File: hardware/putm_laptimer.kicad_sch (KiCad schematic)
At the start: 46 parts, among them J1 Conn_01x22, J10 Conn_01x07, J11 Conn_01x07, J12 Conn_01x09, J13 Conn_01x01, J14 Conn_01x01, J15 Conn_01x01, J16 Conn_01x01, J2 Conn_01x22, J3 Conn_01x22, J4 Conn_01x22, J5 2601-3109, J6 2601-3109, J7 Conn_02x05_Odd_Even, J8 2601-1103, J9 2601-1102

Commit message: Fixed bom table
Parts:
- C1, C10, C3, C4, C5, C6, C7, C8, C9: Mouser Part Number 81-GRM33R6YA104ME14D -> (none); Mouser/TME part number (none) -> 81-GRM33R6YA104ME14D
- D1: Mouser Part Number 621-DESD3V3L2BTQ-7 -> (none); Mouser/TME part number (none) -> 621-DESD3V3L2BTQ-7
- D2: Mouser Part Number 621-MBR230S1F-7 -> (none); Mouser/TME part number (none) -> 621-MBR230S1F-7
- J1, J2, J3, J4: Mouser Part Number ZL262-40SG -> (none); Mouser/TME part number (none) -> ZL262-40SG
- J10, J11: Mouser Part Number ZL262-7SG -> (none); Mouser/TME part number (none) -> ZL262-7SG
- J12: Mouser Part Number ZL262-9SG -> (none); Mouser/TME part number (none) -> ZL262-9SG
- J13, J14, J15, J16: Link (none) -> -
- J7: Mouser Part Number MX-70246-1004 -> (none); Mouser/TME part number (none) -> MX-70246-1004
- R1, R11, R13, R15, R17, R19, R5, R7, R9: Mouser Part Number 652-CR0603FX-1001ELF -> (none); Mouser/TME part number (none) -> 652-CR0603FX-1001ELF
- R10, R12, R14, R16, R18, R2, R20, R6, R8: Mouser Part Number 652-CR0603FX-1002ELF -> (none); Mouser/TME part number (none) -> 652-CR0603FX-1002ELF
- R21: Mouser Part Number 652-CR0603FX-3300ELF -> (none); Mouser/TME part number (none) -> 652-CR0603FX-3300ELF
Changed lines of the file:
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@@
 			)
 		)
-		(property "Mouser Part Number" "ZL262-7SG"
+		(property "Mouser/TME part number" "ZL262-7SG"
 			(at 48.26 170.18 0)
 			(effects
@@
 			)
 		)
-		(property "Mouser Part Number" "621-MBR230S1F-7"
-			(at 163.83 -388.24 0)
-			(effects
-				(font
-					(size 1.27 1.27)
-				)
-				(justify left top)
-				(hide yes)
-			)
-		)
 		(property "Mouser Price/Stock" "https://www.mouser.co.uk/ProductDetail/Diodes-Incorporated/MBR230S1F-7?qs=5V6w%252Be2aIqaf4rGxjeeHeQ%3D%3D"
 			(at 163.83 -488.24 0)
@@
 			)
 		)
+		(property "Mouser/TME part number" "621-MBR230S1F-7"
+			(at 175.26 109.22 0)
+			(effects
+				(font
+					(size 1.27 1.27)
+				)
+				(hide yes)
+			)
+		)
 		(pin "1"
 		)
@@
 			)
 		)
-		(property "Mouser Part Number" "MX-70246-1004"
+		(property "Mouser/TME part number" "MX-70246-1004"
 			(at 170.18 33.02 0)
 			(effects
@@
 			)
 		)
-		(property "Mouser Part Number" "ZL262-7SG"
+		(property "Mouser/TME part number" "ZL262-7SG"
 			(at 33.02 170.18 0)
 			(effects
@@
 			)
 		)
-		(property "Mouser Part Number" "652-CR0603FX-1002ELF "
+		(property "Mouser/TME part number" "652-CR0603FX-1002ELF "
 			(at 80.01 88.9 0)
 			(effects
@@
 			)
 		)
-		(property "Mouser Part Number" "652-CR0603FX-1002ELF "
+		(property "Mouser/TME part number" "652-CR0603FX-1002ELF "
 			(at 189.23 57.15 0)
 			(effects
@@
 			)
 		)
-		(property "Mouser Part Number" "81-GRM33R6YA104ME14D "
+		(property "Mouser/TME part number" "81-GRM33R6YA104ME14D "
 			(at 80.01 69.85 0)
 			(effects
@@
 			)
 		)
-		(property "Mouser Part Number" "81-GRM33R6YA104ME14D "
+		(property "Mouser/TME part number" "81-GRM33R6YA104ME14D "
 			(at 80.01 38.1 0)
 			(effects
@@
 			)
 		)
-		(property "Link" ""
+		(property "Link" "-"
 			(at 165.1 143.51 0)
 			(effects
@@
 			)
 		)
-		(property "Mouser Part Number" "652-CR0603FX-1001ELF "
+		(property "Mouser/TME part number" "652-CR0603FX-1001ELF "
 			(at 114.3 31.75 90)
 			(effects
@@
 			)
 		)
-		(property "Mouser Part Number" "652-CR0603FX-1001ELF "
+		(property "Mouser/TME part number" "652-CR0603FX-1001ELF "
 			(at 182.88 63.5 90)
 			(effects
@@
 			)
 		)
-		(property "Mouser Part Number" "652-CR0603FX-1002ELF "
+		(property "Mouser/TME part number" "652-CR0603FX-1002ELF "
 			(at 80.01 120.65 0)
 			(effects
@@
 			)
 		)
-		(property "Mouser Part Number" "652-CR0603FX-1001ELF "
+		(property "Mouser/TME part number" "652-CR0603FX-1001ELF "
 			(at 114.3 127 90)
 			(effects
@@
 			)
 		)
-		(property "Mouser Part Number" "ZL262-40SG"
+		(property "Mouser/TME part number" "ZL262-40SG"
 			(at 238.76 128.27 0)
 			(effects
@@
 			)
 		)
-		(property "Mouser Part Number" "652-CR0603FX-1001ELF "
+		(property "Mouser/TME part number" "652-CR0603FX-1001ELF "
 			(at 73.66 31.75 90)
 			(effects
@@
 			)
 		)
-		(property "Mouser Part Number" "652-CR0603FX-1002ELF "
+		(property "Mouser/TME part number" "652-CR0603FX-1002ELF "
 			(at 120.65 25.4 0)
 			(effects
@@
 			)
 		)
-		(property "Link" ""
+		(property "Link" "-"
 			(at 165.1 148.59 0)
 			(effects
@@
 			)
 		)
-		(property "Mouser Part Number" "652-CR0603FX-1001ELF "
+		(property "Mouser/TME part number" "652-CR0603FX-1001ELF "
 			(at 114.3 63.5 90)
 			(effects
@@
 			)
 		)
-		(property "Mouser Part Number" "81-GRM33R6YA104ME14D "
+		(property "Mouser/TME part number" "81-GRM33R6YA104ME14D "
 			(at 120.65 101.6 0)
 			(effects
@@
 			)
 		)
-		(property "Mouser Part Number" "ZL262-40SG"
+		(property "Mouser/TME part number" "ZL262-40SG"
 			(at 256.54 128.27 0)
 			(effects
@@
 			)
 		)
-		(property "Mouser Part Number" "81-GRM33R6YA104ME14D "
+		(property "Mouser/TME part number" "81-GRM33R6YA104ME14D "
 			(at 120.65 38.1 0)
 			(effects
@@
 			)
 		)
-		(property "Link" ""
+		(property "Link" "-"
 			(at 165.1 151.13 0)
 			(effects
@@
 			)
 		)
-		(property "Mouser Part Number" "ZL262-40SG"
+		(property "Mouser/TME part number" "ZL262-40SG"
 			(at 256.54 57.15 0)
 			(effects
@@
 			)
 		)
-		(property "Mouser Part Number" "652-CR0603FX-1002ELF "
+		(property "Mouser/TME part number" "652-CR0603FX-1002ELF "
 			(at 120.65 57.15 0)
 			(effects
@@
 			)
 		)
-		(property "Mouser Part Number" "652-CR0603FX-1002ELF "
+		(property "Mouser/TME part number" "652-CR0603FX-1002ELF "
 			(at 80.01 57.15 0)
 			(effects
@@
 			)
 		)
-		(property "Mouser Part Number" "ZL262-40SG"
+		(property "Mouser/TME part number" "ZL262-40SG"
 			(at 238.76 57.15 0)
 			(effects
@@
 			)
 		)
-		(property "Mouser Part Number" "652-CR0603FX-1001ELF "
+		(property "Mouser/TME part number" "652-CR0603FX-1001ELF "
 			(at 73.66 127 90)
 			(effects
@@
 			)
 		)
-		(property "Mouser Part Number" "ZL262-9SG"
+		(property "Mouser/TME part number" "ZL262-9SG"
 			(at 97.79 172.72 0)
 			(effects
@@
 			)
 		)
-		(property "Mouser Part Number" "652-CR0603FX-1001ELF "
+		(property "Mouser/TME part number" "652-CR0603FX-1001ELF "
 			(at 114.3 95.25 90)
 			(effects
@@
 			)
 		)
-		(property "Mouser Part Number" "81-GRM33R6YA104ME14D "
+		(property "Mouser/TME part number" "81-GRM33R6YA104ME14D "
 			(at 80.01 101.6 0)
 			(effects
@@
 			)
 		)
-		(property "Mouser Part Number" "652-CR0603FX-1002ELF "
+		(property "Mouser/TME part number" "652-CR0603FX-1002ELF "
 			(at 120.65 88.9 0)
 			(effects
@@
 			)
 		)
-		(property "Mouser Part Number" "652-CR0603FX-1001ELF "
+		(property "Mouser/TME part number" "652-CR0603FX-1001ELF "
 			(at 73.66 63.5 90)
 			(effects
@@
 			)
 		)
-		(property "Mouser Part Number" "652-CR0603FX-1001ELF "
+		(property "Mouser/TME part number" "652-CR0603FX-1001ELF "
 			(at 73.66 95.25 90)
 			(effects
@@
 			)
 		)
-		(property "Mouser Part Number" "81-GRM33R6YA104ME14D "
+		(property "Mouser/TME part number" "81-GRM33R6YA104ME14D "
 			(at 80.01 133.35 0)
 			(effects
@@
 			)
 		)
-		(property "Mouser Part Number" "81-GRM33R6YA104ME14D "
+		(property "Mouser/TME part number" "81-GRM33R6YA104ME14D "
 			(at 120.65 69.85 0)
 			(effects
@@
 			)
 		)
-		(property "Mouser Part Number" "652-CR0603FX-1002ELF "
+		(property "Mouser/TME part number" "652-CR0603FX-1002ELF "
 			(at 80.01 25.4 0)
 			(effects
@@
 			)
 		)
-		(property "Link" ""
+		(property "Link" "-"
 			(at 165.1 146.05 0)
 			(effects
@@
 			)
 		)
-		(property "Mouser Part Number" "81-GRM33R6YA104ME14D "
+		(property "Mouser/TME part number" "81-GRM33R6YA104ME14D "
 			(at 120.65 133.35 0)
 			(effects
@@
 			)
 		)
-		(property "Mouser Part Number" "652-CR0603FX-3300ELF "
+		(property "Mouser/TME part number" "652-CR0603FX-3300ELF "
 			(at 44.45 69.85 90)
 			(effects
@@
 			)
 		)
-		(property "Mouser Part Number" "81-GRM33R6YA104ME14D "
+		(property "Mouser/TME part number" "81-GRM33R6YA104ME14D "
 			(at 189.23 69.85 0)
 			(effects
@@
 			)
 		)
-		(property "Mouser Part Number" "652-CR0603FX-1002ELF "
+		(property "Mouser/TME part number" "652-CR0603FX-1002ELF "
 			(at 120.65 120.65 0)
 			(effects
@@
 			)
 		)
-		(property "Mouser Part Number" "621-DESD3V3L2BTQ-7 "
-			(at 181.61 571.12 0)
-			(effects
-				(font
-					(size 1.27 1.27)
-				)
-				(justify left top)
-				(hide yes)
-			)
-		)
 		(property "Mouser Price/Stock" ""
 			(at 181.61 671.12 0)
@@
 			(at 165.1 76.2 0)
 			(effects
+				(font
+					(size 1.27 1.27)
+				)
+				(hide yes)
+			)
+		)
+		(property "Mouser/TME part number" "621-DESD3V3L2BTQ-7 "
+			(at 165.1 76.2 0)
+			(effects

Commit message: Table part numbers fix
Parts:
- C1, C10, C3, C4, C5, C6, C7, C8, C9: Manufacturer_Part_Number (none) -> GRM033R6YA104ME14D
- J1, J2, J3, J4: Manufacturer_Part_Number (none) -> DS1023-1*40S21
- J10, J11: Manufacturer_Part_Number (none) -> DS1023-1*7S21
- J12: Manufacturer_Part_Number (none) -> DS1023-1*9S21
- J13, J14, J15, J16: Manufacturer_Part_Number (none) -> -; Mouser/TME part number (none) -> -
- J5, J6: Manufacturer_Part_Number (none) -> 2601-3109; Mouser/TME part number (none) -> sample
- J7: Link https://www.tme.eu/pl/details/mx-70246-1004/zlacza-pozostal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 -> https://www.tme.eu/pl/details/zl231-10pg/zlacza-idc/connfly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; Manufacturer_Part_Number (none) -> DS1013-10SSIB1-B-0; Mouser/TME part number MX-70246-1004 -> ZL231-10PG
- J8: Manufacturer_Part_Number (none) -> 2601-1103; Mouser/TME part number (none) -> sample
- J9: Manufacturer_Part_Number (none) -> 2601-1102; Mouser/TME part number (none) -> sample
- R1, R11, R13, R15, R17, R19, R5, R7, R9: Manufacturer_Part_Number (none) -> CR0603-FX-1001ELF
- R10, R12, R14, R16, R18, R2, R20, R6, R8: Manufacturer_Part_Number (none) -> CR0603-FX-1002ELF
- R21: Manufacturer_Part_Number (none) -> CR0603-FX-3300ELF

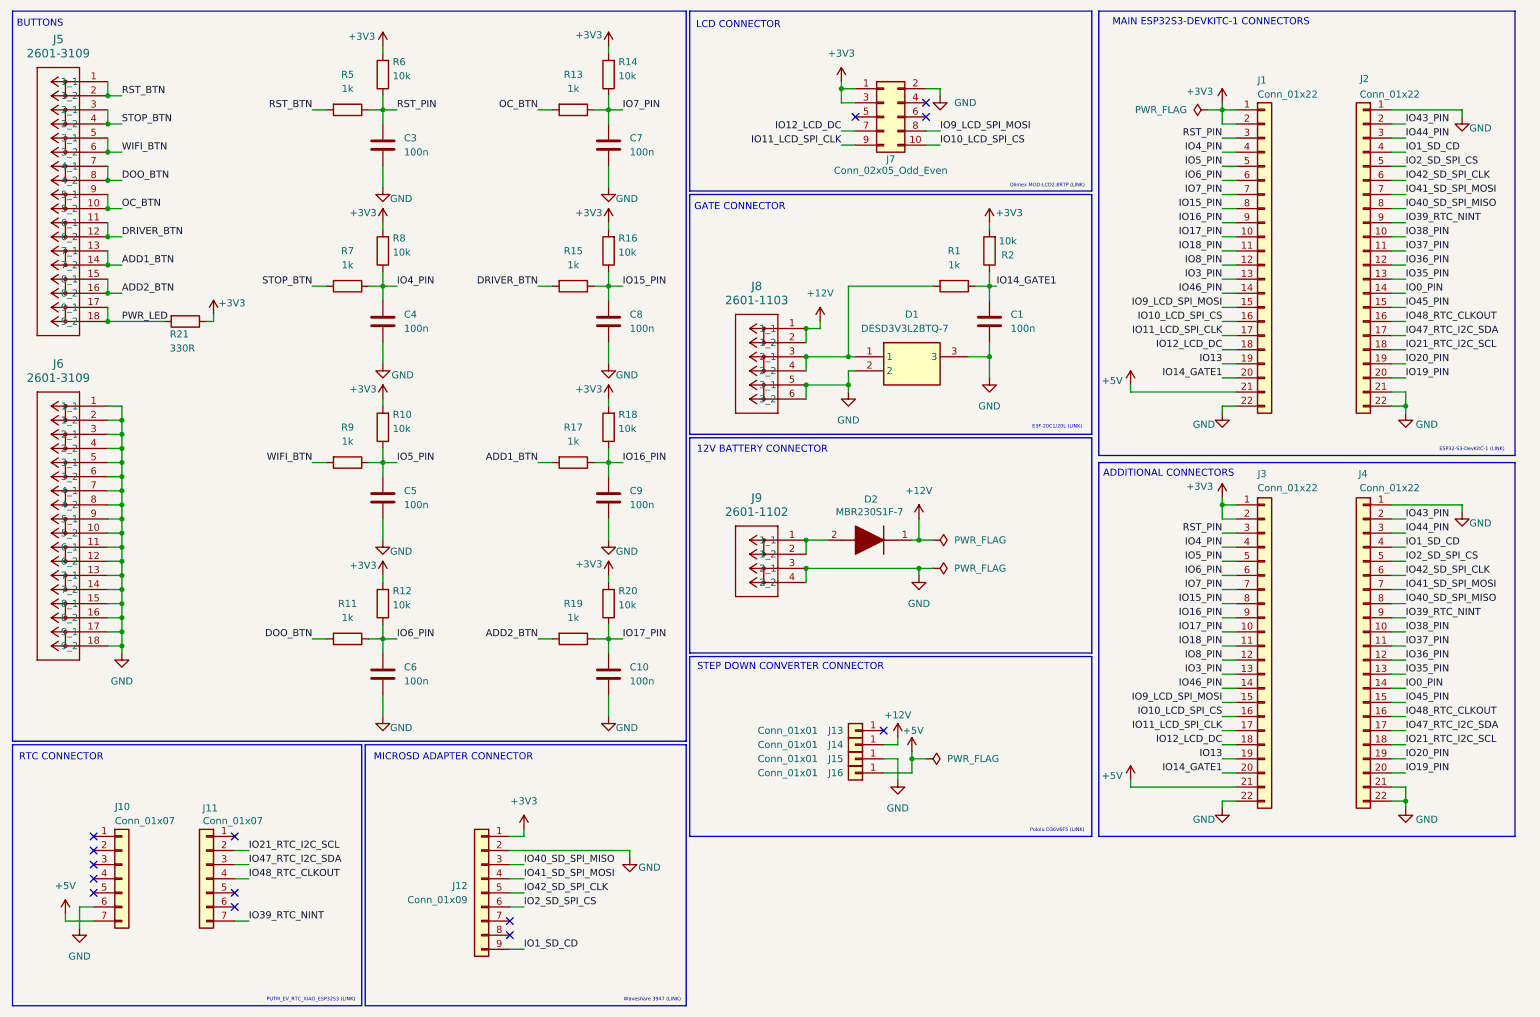
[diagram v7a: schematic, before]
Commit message: Added second gate connector
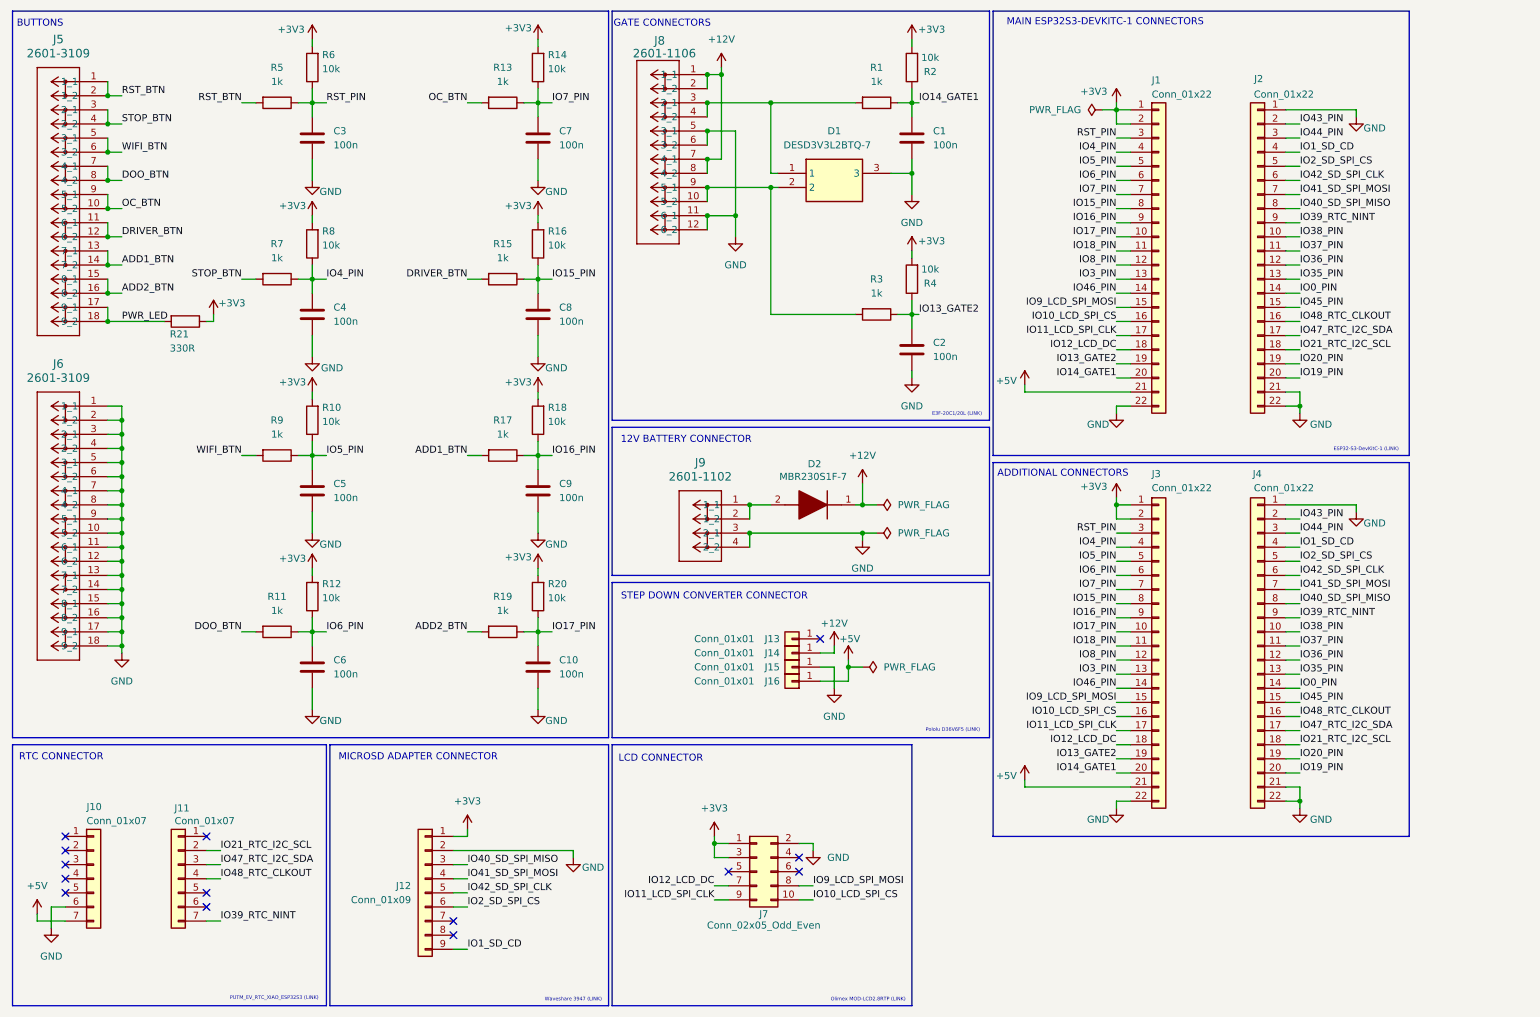
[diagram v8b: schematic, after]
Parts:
- removed J8: 2601-1103, Footprint:CONN3_2601-1103_WAG, symbol 2026-02-04_11-25-15:2601-1103
- added C2: 100n, Capacitor_SMD:C_0603_1608Metric, symbol Device:C
- added J8: 2601-1106, Footprint:CONN6_2601-1106_WAG, symbol 2026-02-19_19-34-36:2601-1106
- added R3: 1k, Resistor_SMD:R_0603_1608Metric, symbol Device:R
- added R4: 10k, Resistor_SMD:R_0603_1608Metric, symbol Device:R
- J7: footprint Connector_PinHeader_2.54mm:PinHeader_2x05_P2.54mm_Vertical_SMD -> Connector_PinHeader_2.54mm:PinHeader_2x05_P2.54mm_Vertical
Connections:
- net +12V: now also J8.1 (1_1), J8.2 (1_2), J8.7 (4_1), J8.8 (4_2)
- net +3V3: now also R4.2
- net GND: now also C2.2, J8.11 (6_1), J8.12 (6_2), J8.5 (3_1), J8.6 (3_2); no longer D1.2
- net at D1.1, R1.2: now also J8.3 (2_1), J8.4 (2_2)
- net IO13 renamed IO13_GATE2
- net IO13_GATE2: now also C2.1, R3.1, R4.1
- new net: D1.2, J8.10 (5_2), J8.9 (5_1), R3.2
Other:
- note added: "GATE CONNECTORS"
- note removed: "GATE CONNECTOR"
- moved on the sheet: C1, C10, C3, C4, C5, C6, C7, C8, C9, D1, D2, J1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
